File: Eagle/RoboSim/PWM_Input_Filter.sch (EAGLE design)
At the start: 72 parts, among them IC1 TLV2772, IC2 TLV2772, IC3 TLV2772

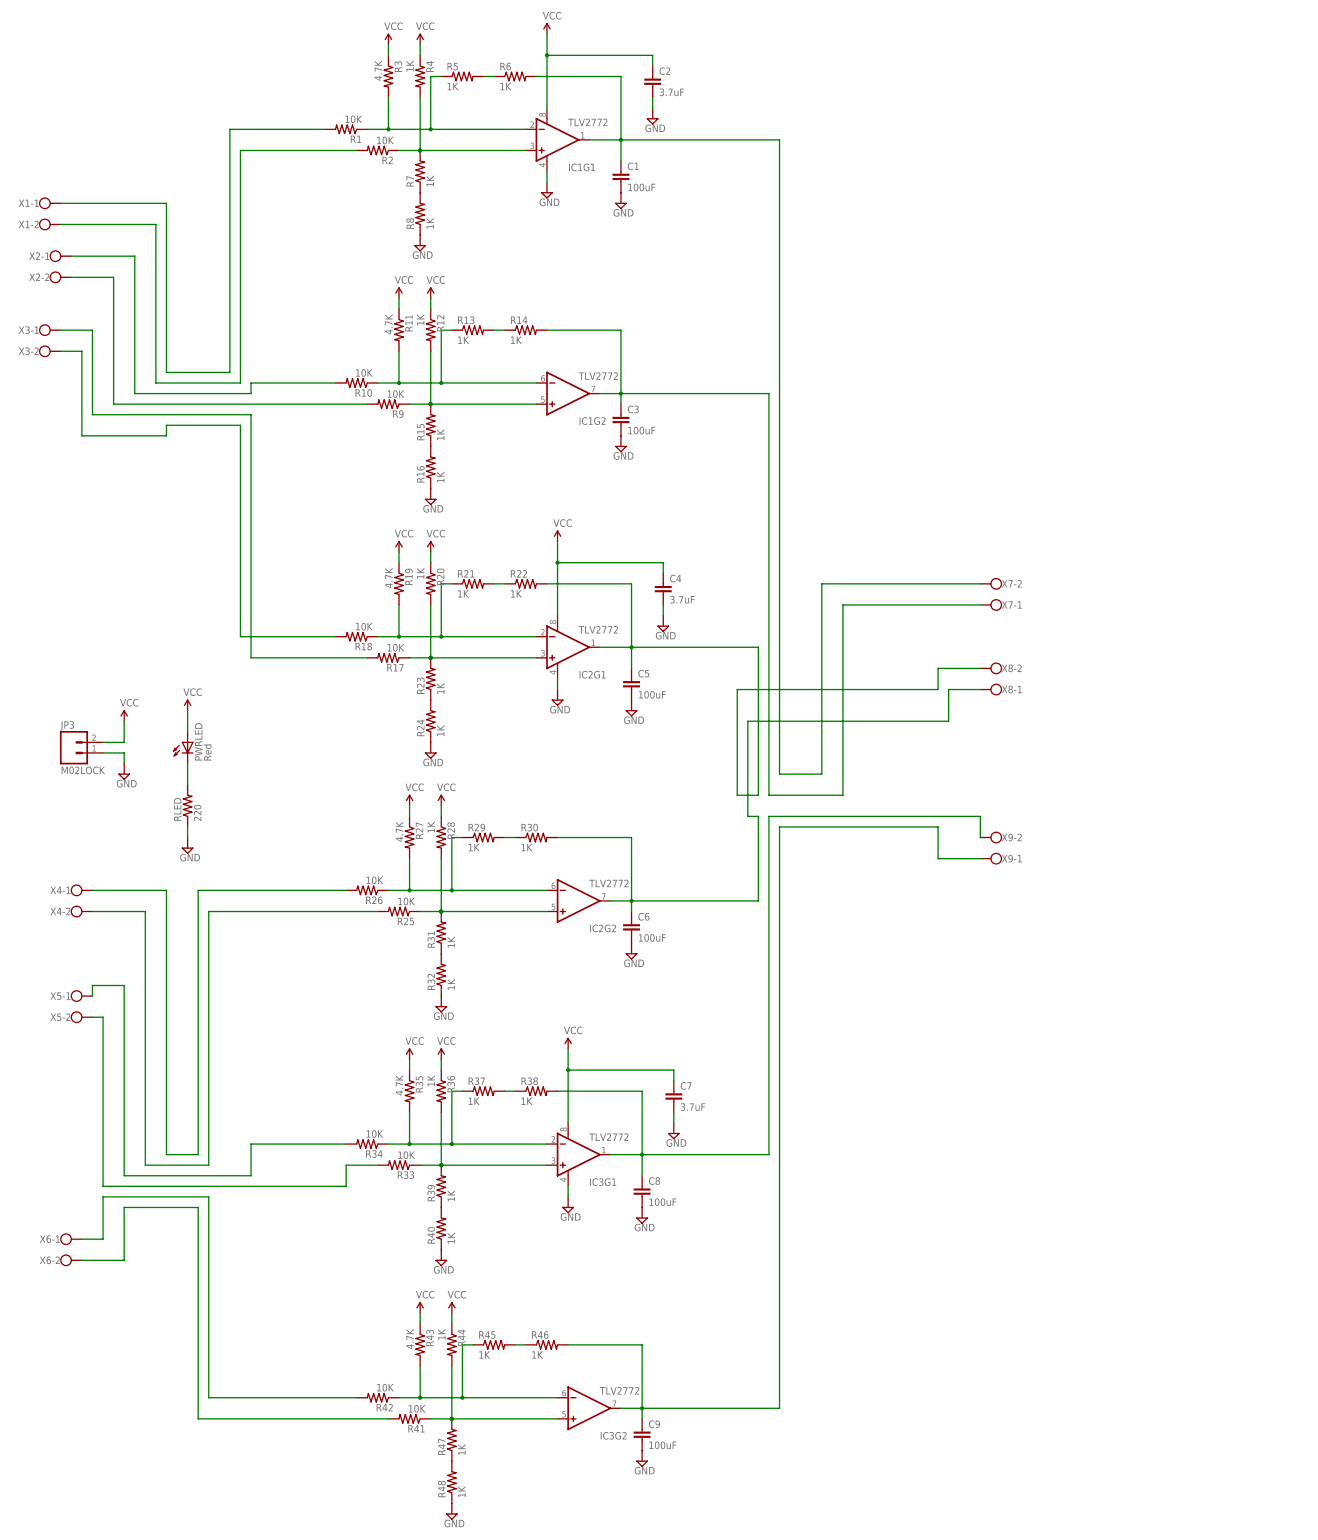
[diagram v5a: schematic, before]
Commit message: trimmed pwm filter circuit schematic to just show two channels, fixed up schematic
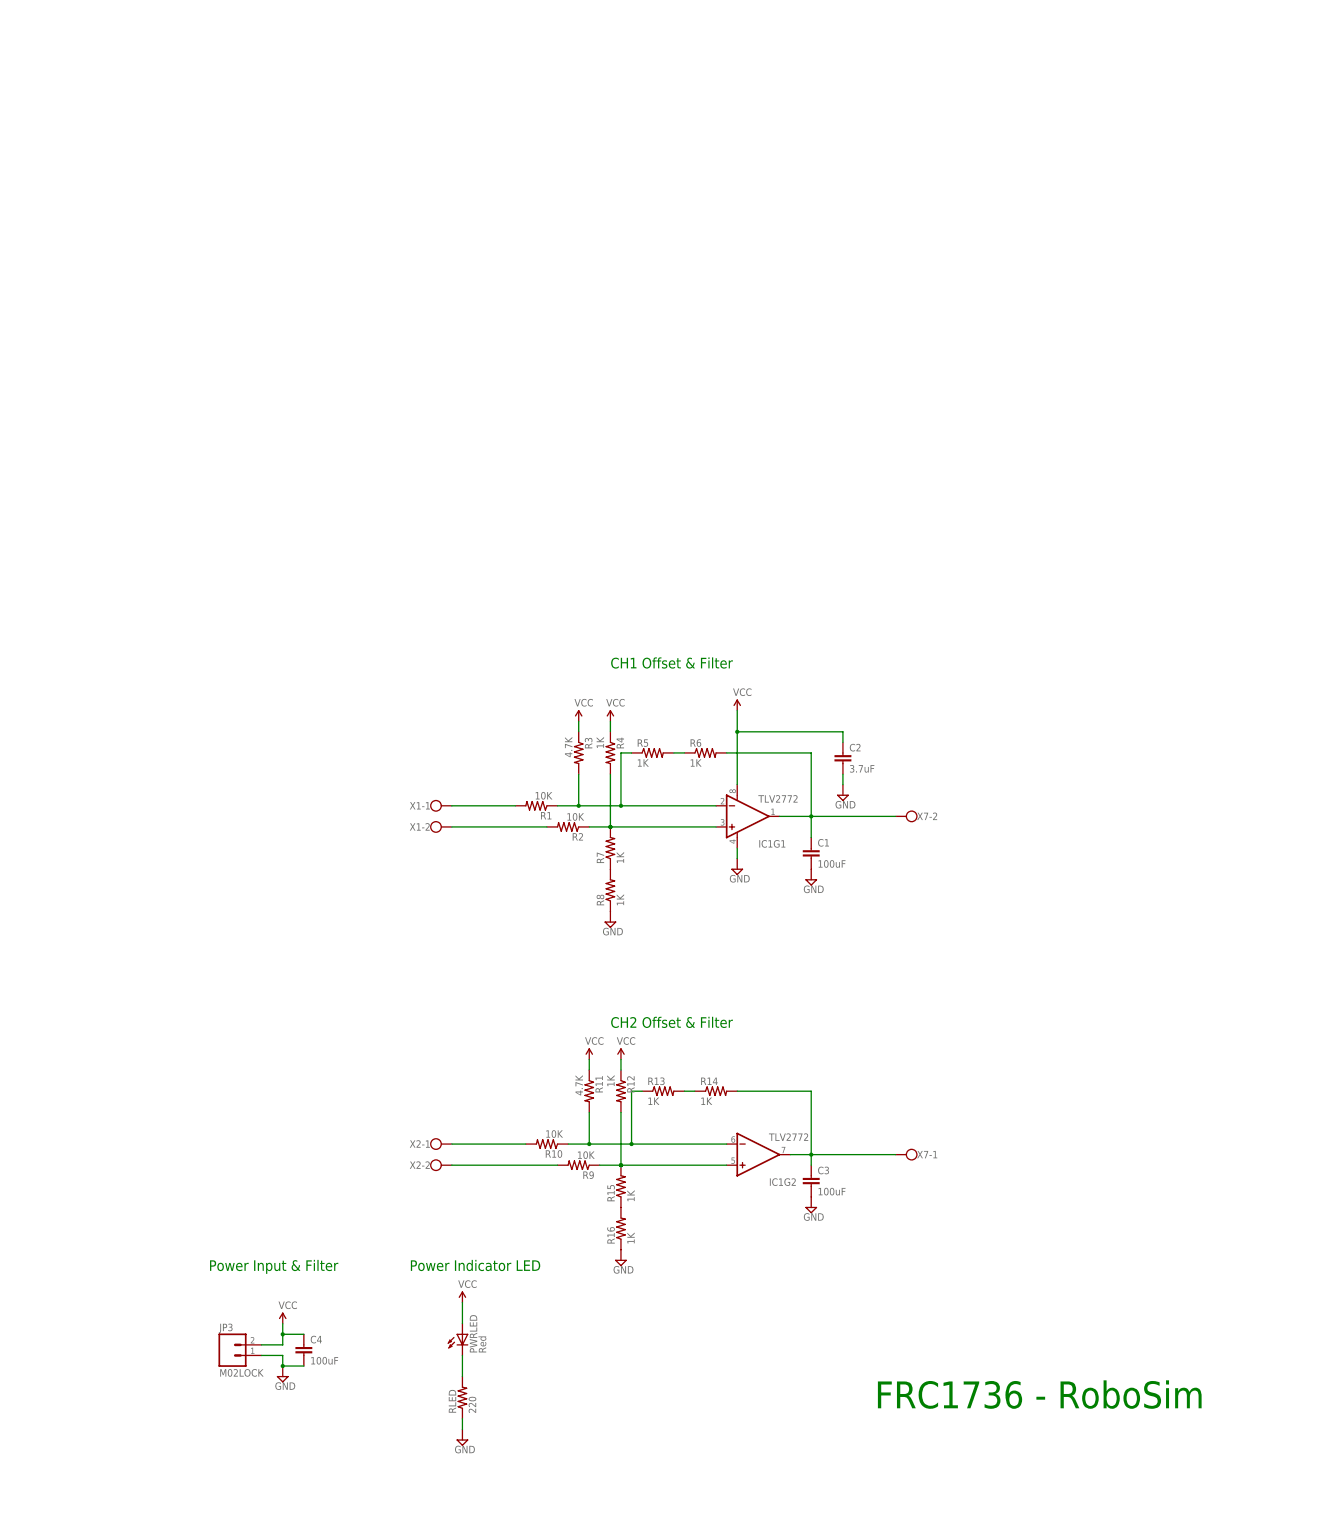
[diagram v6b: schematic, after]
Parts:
- removed C5, C6, C8, C9: 100uF, SparkFun-Passives:CAPPTH
- removed C7: 3.7uF, SparkFun-Passives:CAPPTH
- removed IC2, IC3: TLV2772, SparkFun-AnalogIC:LM358
- removed R17, R18, R25, R26, R33, R34, R41, R42: 10K, SparkFun-Passives:RESISTOR1206
- removed R19, R27, R35, R43: 4.7K, SparkFun-Passives:RESISTOR1206
- removed R20, R21, R22, R23, R24, R28, R29, R30, R31, R32, R36, R37, R38, R39, R40, R44, R45, R46, R47, R48: 1K, SparkFun-Passives:RESISTOR1206
- removed X3, X4, X5, X6, X8, X9: (no value), con-wago-500:W237-102
- C4: value 3.7uF -> 100uF
- R1, R10, R11, R12, R13, R14, R15, R16, R2, R3, R4, R5, R6, R7, R8, R9, RLED: device SparkFun-Passives:RESISTOR1206 -> SparkFun-Passives:RESISTORAXIAL-0.3
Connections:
- removed net N$16: R18.2, X3-2.KL
- removed net N$18: C6.1, IC2G2.OUT, R30.2, X8-1.KL
- removed net N$2: R17.2, X3-1.KL
- removed net N$20: R25.2, X4-2.KL
- removed net N$22: R26.2, X4-1.KL
- removed net N$24: IC2G1.-IN, R18.1, R19.2, R21.1
- removed net N$25: IC2G1.+IN, R17.1, R20.2, R23.2
- removed net N$26: R21.2, R22.1
- removed net N$27: R23.1, R24.2
- removed net N$28: IC2G2.-IN, R26.1, R27.2, R29.1
- removed net N$29: IC2G2.+IN, R25.1, R28.2, R31.2
- removed net N$30: R34.2, X5-1.KL
- removed net N$31: R33.2, X5-2.KL
- removed net N$32: R29.2, R30.1
- removed net N$34: R41.2, X6-2.KL
- removed net N$36: R31.1, R32.2
- removed net N$37: C5.1, IC2G1.OUT, R22.2, X8-2.KL
- removed net N$40: C9.1, IC3G2.OUT, R46.2, X9-1.KL
- removed net N$41: R42.2, X6-1.KL
- removed net N$43: IC3G1.-IN, R34.1, R35.2, R37.1
- removed net N$45: IC3G1.+IN, R33.1, R36.2, R39.2
- removed net N$46: R37.2, R38.1
- removed net N$47: R39.1, R40.2
- removed net N$48: IC3G2.-IN, R42.1, R43.2, R45.1
- removed net N$49: IC3G2.+IN, R41.1, R44.2, R47.2
- removed net N$50: R45.2, R46.1
- removed net N$51: R47.1, R48.2
- removed net N$52: C8.1, IC3G1.OUT, R38.2, X9-2.KL
- net GND: no longer C5.2, C6.2, C7.2, C8.2, C9.2, IC2G1.V-, IC3G1.V-, R24.1, R32.1, R40.1, R48.1
- net VCC: no longer C7.1, IC2G1.V+, IC3G1.V+, R19.1, R20.1, R27.1, R28.1, R35.1, R36.1, R43.1, R44.1
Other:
- note added: "CH1 Offset & Filter"
- note added: "CH2 Offset & Filter"
- note added: "FRC1736 - RoboSim"
- note added: "Power Indicator LED"
- note added: "Power Input & Filter"
- moved on the sheet: C1, C2, C3, C4, IC1G1, IC1G2, JP3, PWRLED, R1, R10, R11, R12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

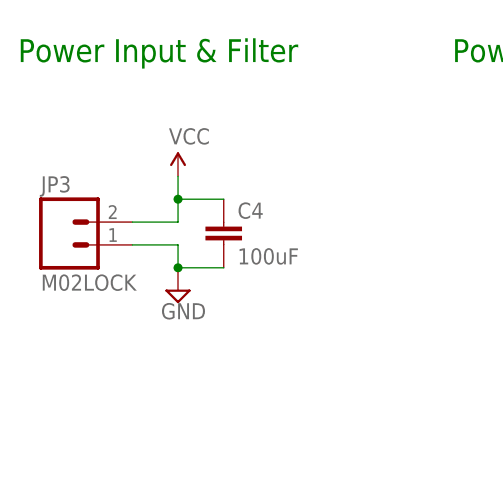
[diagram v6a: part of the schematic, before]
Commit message: added extra text to schematic
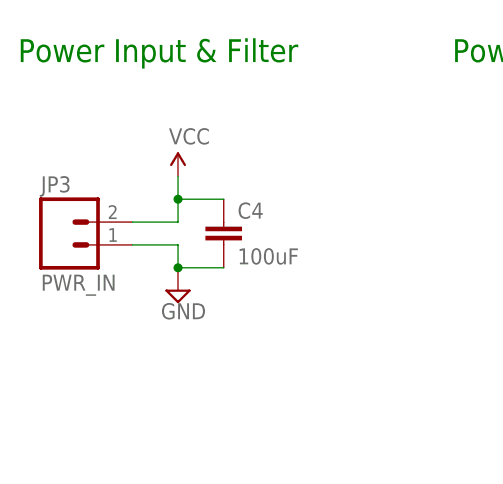
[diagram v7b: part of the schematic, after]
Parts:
- JP3: value M02LOCK -> PWR_IN
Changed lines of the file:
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@@
 <grid distance="0.1" unitdist="inch" unit="inch" style="lines" multiple="1" display="no" altdistance="0.01" altunitdist="inch" altunit="inch"/>
 <layers>
-<layer number="1" name="Top" color="4" fill="1" visible="yes" active="no"/>
-<layer number="16" name="Bottom" color="1" fill="1" visible="yes" active="no"/>
-<layer number="17" name="Pads" color="2" fill="1" visible="yes" active="no"/>
-<layer number="18" name="Vias" color="2" fill="1" visible="yes" active="no"/>
-<layer number="19" name="Unrouted" color="6" fill="1" visible="yes" active="no"/>
-<layer number="20" name="Dimension" color="15" fill="1" visible="yes" active="no"/>
-<layer number="21" name="tPlace" color="7" fill="1" visible="yes" active="no"/>
-<layer number="22" name="bPlace" color="7" fill="1" visible="yes" active="no"/>
-<layer number="23" name="tOrigins" color="15" fill="1" visible="yes" active="no"/>
-<layer number="24" name="bOrigins" color="15" fill="1" visible="yes" active="no"/>
-<layer number="25" name="tNames" color="7" fill="1" visible="yes" active="no"/>
-<layer number="26" name="bNames" color="7" fill="1" visible="yes" active="no"/>
-<layer number="27" name="tValues" color="7" fill="1" visible="yes" active="no"/>
-<layer number="28" name="bValues" color="7" fill="1" visible="yes" active="no"/>
+<layer number="1" name="Top" color="4" fill="1" visible="no" active="no"/>
+<layer number="16" name="Bottom" color="1" fill="1" visible="no" active="no"/>
+<layer number="17" name="Pads" color="2" fill="1" visible="no" active="no"/>
+<layer number="18" name="Vias" color="2" fill="1" visible="no" active="no"/>
+<layer number="19" name="Unrouted" color="6" fill="1" visible="no" active="no"/>
+<layer number="20" name="Dimension" color="15" fill="1" visible="no" active="no"/>
+<layer number="21" name="tPlace" color="7" fill="1" visible="no" active="no"/>
+<layer number="22" name="bPlace" color="7" fill="1" visible="no" active="no"/>
+<layer number="23" name="tOrigins" color="15" fill="1" visible="no" active="no"/>
+<layer number="24" name="bOrigins" color="15" fill="1" visible="no" active="no"/>
+<layer number="25" name="tNames" color="7" fill="1" visible="no" active="no"/>
+<layer number="26" name="bNames" color="7" fill="1" visible="no" active="no"/>
+<layer number="27" name="tValues" color="7" fill="1" visible="no" active="no"/>
+<layer number="28" name="bValues" color="7" fill="1" visible="no" active="no"/>
 <layer number="29" name="tStop" color="7" fill="3" visible="no" active="no"/>
 <layer number="30" name="bStop" color="7" fill="6" visible="no" active="no"/>
@@
 <layer number="35" name="tGlue" color="7" fill="4" visible="no" active="no"/>
 <layer number="36" name="bGlue" color="7" fill="5" visible="no" active="no"/>
-<layer number="37" name="tTest" color="7" fill="1" visible="yes" active="no"/>
-<layer number="38" name="bTest" color="7" fill="1" visible="yes" active="no"/>
+<layer number="37" name="tTest" color="7" fill="1" visible="no" active="no"/>
+<layer number="38" name="bTest" color="7" fill="1" visible="no" active="no"/>
 <layer number="39" name="tKeepout" color="4" fill="11" visible="no" active="no"/>
 <layer number="40" name="bKeepout" color="1" fill="11" visible="no" active="no"/>
@@
 <layer number="44" name="Drills" color="7" fill="1" visible="no" active="no"/>
 <layer number="45" name="Holes" color="7" fill="1" visible="no" active="no"/>
-<layer number="46" name="Milling" color="3" fill="1" visible="yes" active="no"/>
-<layer number="47" name="Measures" color="7" fill="1" visible="yes" active="no"/>
-<layer number="48" name="Document" color="7" fill="1" visible="yes" active="no"/>
-<layer number="49" name="Reference" color="7" fill="1" visible="yes" active="no"/>
-<layer number="50" name="dxf" color="7" fill="1" visible="yes" active="no"/>
-<layer number="51" name="tDocu" color="7" fill="1" visible="yes" active="no"/>
-<layer number="52" name="bDocu" color="7" fill="1" visible="yes" active="no"/>
-<layer number="53" name="tGND_GNDA" color="7" fill="9" visible="yes" active="no"/>
-<layer number="54" name="bGND_GNDA" color="1" fill="9" visible="yes" active="no"/>
-<layer number="56" name="wert" color="7" fill="1" visible="yes" active="no"/>
+<layer number="46" name="Milling" color="3" fill="1" visible="no" active="no"/>
+<layer number="47" name="Measures" color="7" fill="1" visible="no" active="no"/>
+<layer number="48" name="Document" color="7" fill="1" visible="no" active="no"/>
+<layer number="49" name="Reference" color="7" fill="1" visible="no" active="no"/>
+<layer number="50" name="dxf" color="7" fill="1" visible="no" active="no"/>
+<layer number="51" name="tDocu" color="7" fill="1" visible="no" active="no"/>
+<layer number="52" name="bDocu" color="7" fill="1" visible="no" active="no"/>
+<layer number="53" name="tGND_GNDA" color="7" fill="9" visible="no" active="no"/>
+<layer number="54" name="bGND_GNDA" color="1" fill="9" visible="no" active="no"/>
+<layer number="56" name="wert" color="7" fill="1" visible="no" active="no"/>
 <layer number="91" name="Nets" color="2" fill="1" visible="yes" active="yes"/>
 <layer number="92" name="Busses" color="1" fill="1" visible="yes" active="yes"/>
@@
 <parts>
 <part name="IC1" library="SparkFun-AnalogIC" deviceset="LM358" device="" value="TLV2772"/>
-<part name="JP3" library="SparkFun-Connectors" deviceset="M02" device="LOCK"/>
+<part name="JP3" library="SparkFun-Connectors" deviceset="M02" device="LOCK" value="PWR_IN"/>
 <part name="SUPPLY1" library="supply2" deviceset="GND" device=""/>
 <part name="SUPPLY2" library="SparkFun-Aesthetics" deviceset="VCC" device=""/>
